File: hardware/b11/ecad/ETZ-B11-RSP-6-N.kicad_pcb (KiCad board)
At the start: 2 copper layers, 144.7 x 90.2 mm, 0 parts

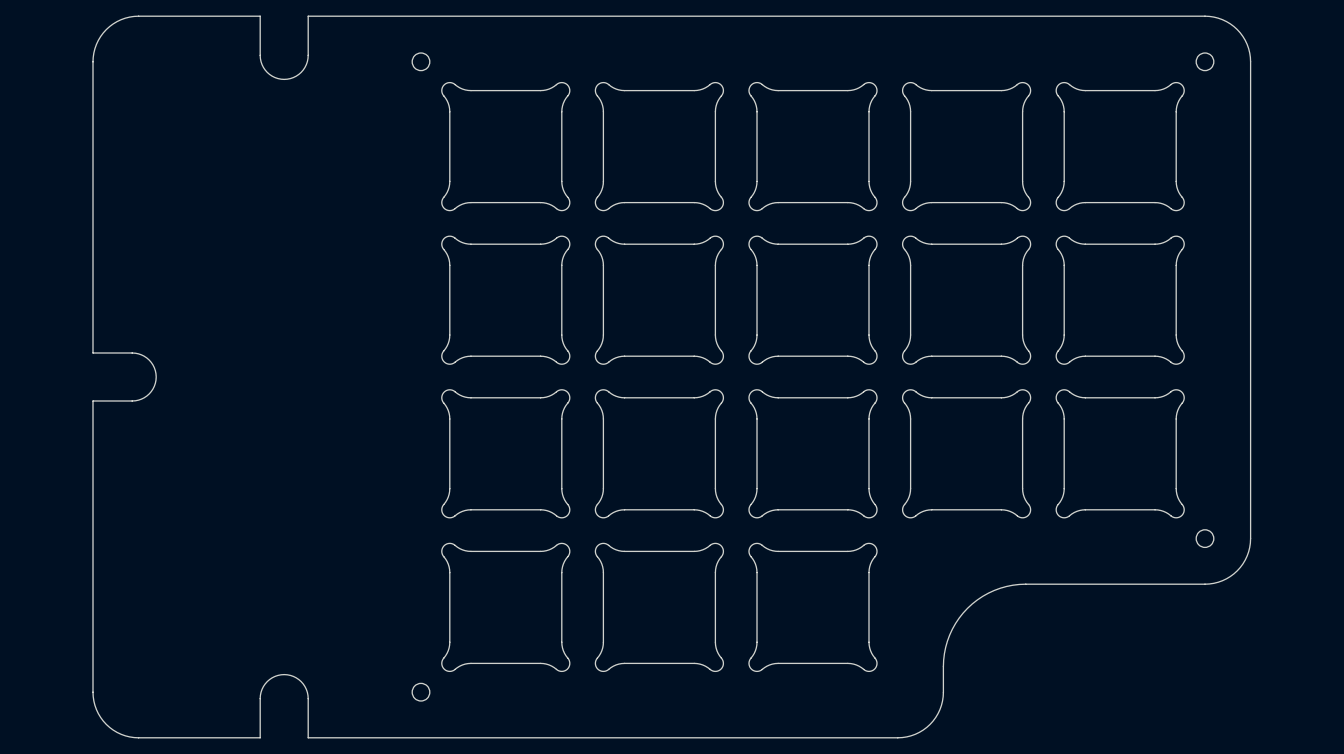
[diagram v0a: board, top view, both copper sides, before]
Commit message: fix(hardware/b11): correct 6-col PCB outlines and regenerate all boards
Update DXF outlines for all 6-col variants (LSC, RSC, LSP, RSP — both
normal and low profile) exported manually from OnShape with the _6
configuration. Regenerate all 16 KiCad PCBs from the corrected outlines
and re-place MX hotswap switches on the 4 normal-profile carrier boards.

Co-Authored-By: Claude Sonnet 4.6 <noreply@anthropic.com>
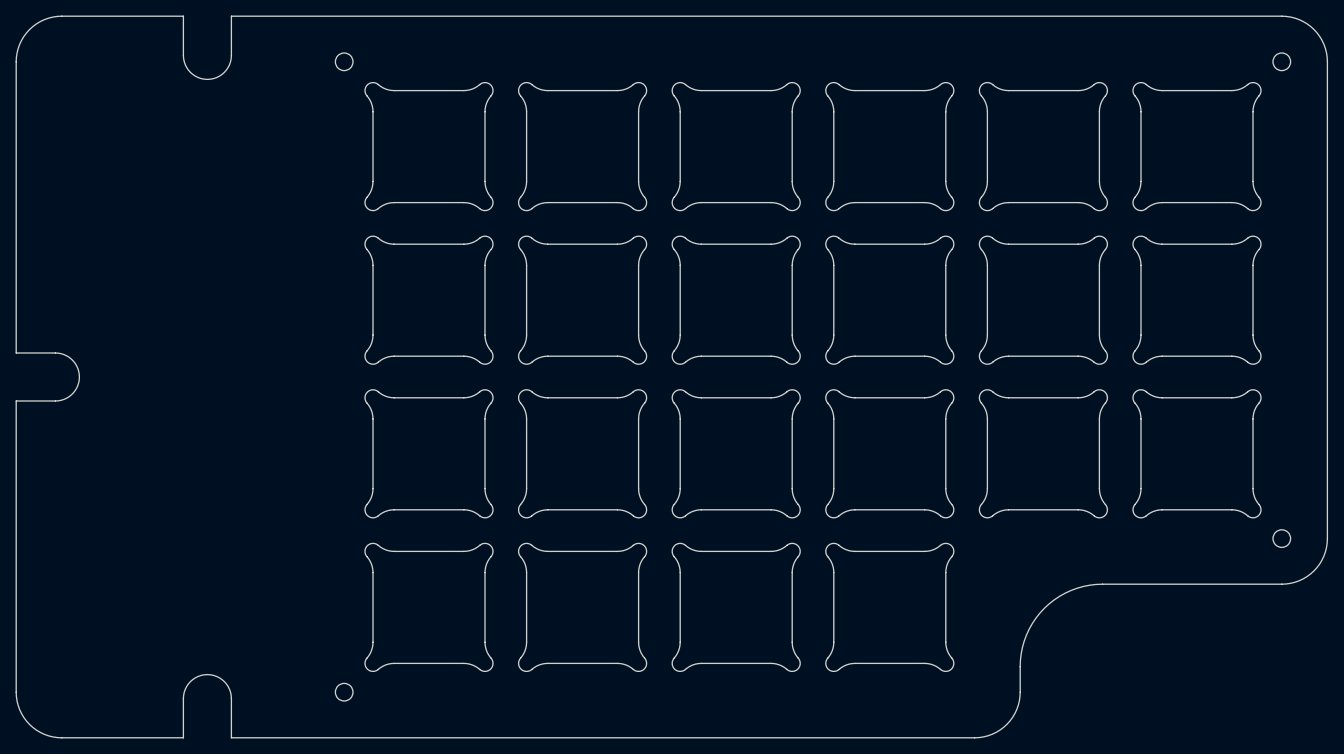
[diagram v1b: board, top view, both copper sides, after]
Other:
- board size 144.7 x 90.2 mm -> 163.9 x 90.2 mm
